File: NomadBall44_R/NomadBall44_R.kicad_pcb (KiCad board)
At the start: 2 copper layers, 147.4 x 96.5 mm, 57 parts, among them SW1 SW_Push, SW10 SW_Push, SW11 SW_Push, SW12 SW_Push, SW13 SW_Push, SW14 SW_Push, SW15 SW_Push, SW16 SW_Push, SW17 SW_Push, SW18 SW_Push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

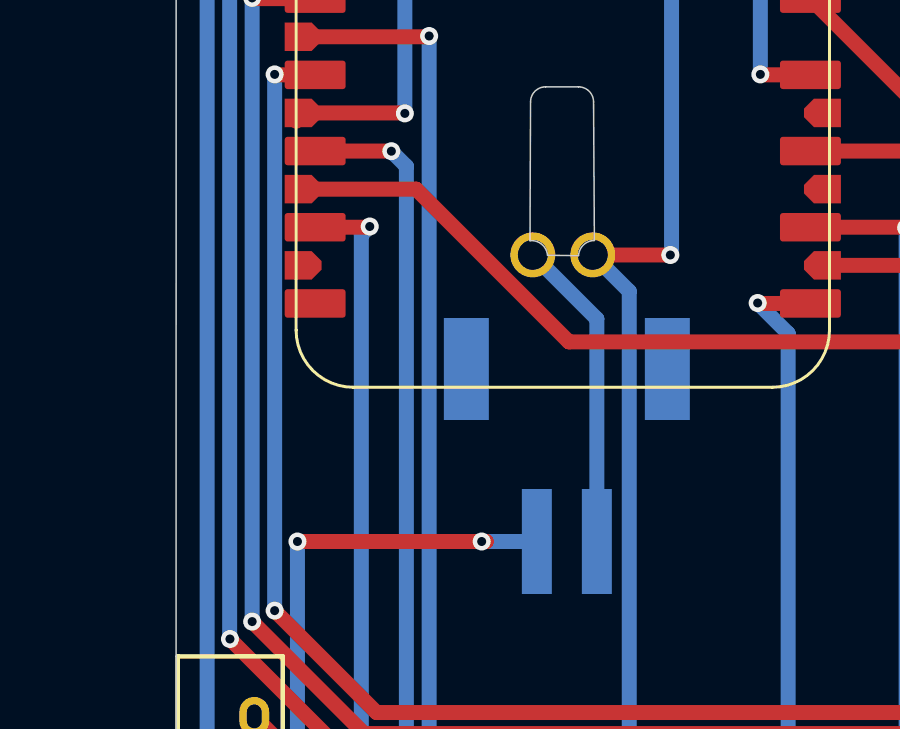
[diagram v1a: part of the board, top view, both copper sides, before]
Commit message: バッテリー周りの配線を修正
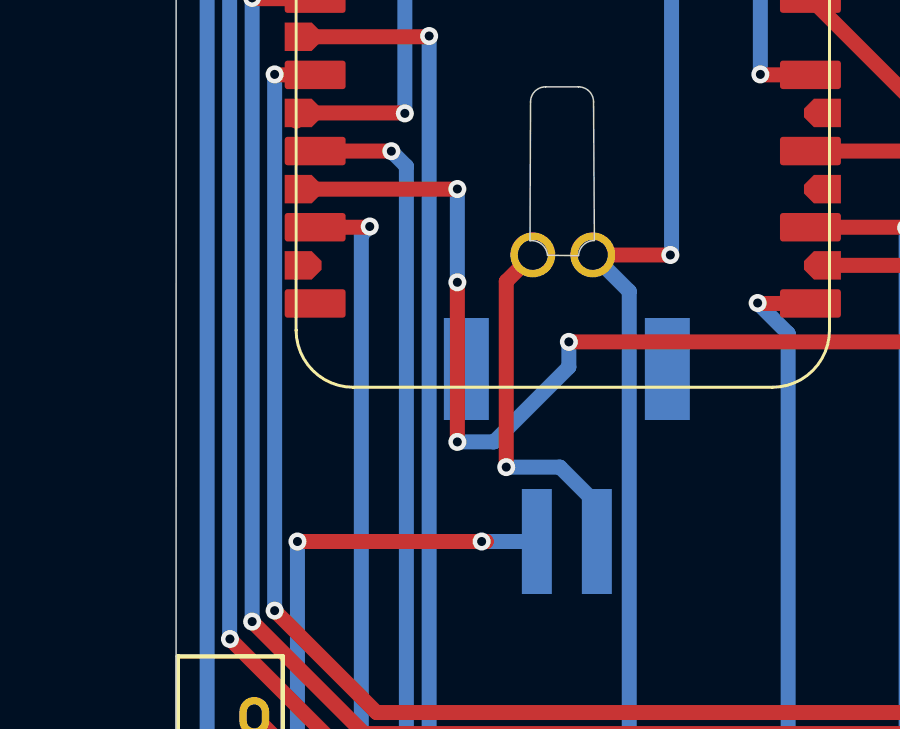
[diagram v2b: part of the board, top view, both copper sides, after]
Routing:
- net Col4: track 150.0 -> 158.2 mm, vias 1 -> 5
- net Bat: track 11.4 -> 13.2 mm, vias 0 -> 1
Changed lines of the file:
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@@
 	)
 	(segment
+		(start 89.98 73.41)
+		(end 89.98 67.22)
+		(width 0.5)
+		(layer "F.Cu")
+		(net 2)
+	)
+	(segment
+		(start 89.98 67.22)
+		(end 90.865 66.335)
+		(width 0.5)
+		(layer "F.Cu")
+		(net 2)
+	)
+	(via
+		(at 89.98 73.41)
+		(size 0.6)
+		(drill 0.3)
+		(layers "F.Cu" "B.Cu")
+		(net 2)
+	)
+	(segment
+		(start 91.77 73.41)
+		(end 89.98 73.41)
+		(width 0.5)
+		(layer "B.Cu")
+		(net 2)
+	)
+	(segment
 		(start 90.865 66.335)
 		(end 90.960327 66.335)
@@
 	)
 	(segment
-		(start 90.985748 66.335)
-		(end 91.103267 66.452519)
+		(start 93 74.64)
+		(end 91.77 73.41)
 		(width 0.5)
 		(layer "B.Cu")
@@
 	)
 	(segment
-		(start 91.103267 66.452519)
-		(end 91.236429 66.588077)
+		(start 90.985748 66.335)
+		(end 91.103267 66.452519)
 		(width 0.5)
 		(layer "B.Cu")
@@
 	)
 	(segment
-		(start 90.865 66.335)
-		(end 90.985748 66.335)
+		(start 93 75.89)
+		(end 93 74.64)
 		(width 0.5)
 		(layer "B.Cu")
@@
 	)
 	(segment
-		(start 93 68.47)
-		(end 93 75.89)
+		(start 91.103267 66.452519)
+		(end 91.236429 66.588077)
 		(width 0.5)
 		(layer "B.Cu")
@@
 	(segment
 		(start 90.865 66.335)
-		(end 93 68.47)
+		(end 90.985748 66.335)
 		(width 0.5)
 		(layer "B.Cu")
@@
 	)
 	(segment
-		(start 86.976529 64.145)
-		(end 92.067529 69.236)
+		(start 88.35 67.25)
+		(end 88.35 72.57)
 		(width 0.5)
 		(layer "F.Cu")
@@
 	)
 	(segment
-		(start 182.427925 67.64)
-		(end 183.58 67.64)
+		(start 83.21 64.145)
+		(end 88.345 64.145)
 		(width 0.5)
 		(layer "F.Cu")
@@
 	)
 	(segment
-		(start 138.196 68.649628)
-		(end 141.145628 65.7)
+		(start 182.427925 67.64)
+		(end 183.58 67.64)
 		(width 0.5)
 		(layer "F.Cu")
@@
 	)
 	(segment
-		(start 83.21 64.145)
-		(end 86.976529 64.145)
+		(start 138.196 68.649628)
+		(end 141.145628 65.7)
 		(width 0.5)
 		(layer "F.Cu")
@@
 		(net 40)
 	)
+	(segment
+		(start 88.345 64.145)
+		(end 88.35 64.14)
+		(width 0.5)
+		(layer "F.Cu")
+		(net 40)
+	)
+	(via
+		(at 92.067529 69.236)
+		(size 0.6)
+		(drill 0.3)
+		(layers "F.Cu" "B.Cu")
+		(net 40)
+	)
+	(via
+		(at 88.35 64.14)
+		(size 0.6)
+		(drill 0.3)
+		(layers "F.Cu" "B.Cu")
+		(net 40)
+	)
+	(via
+		(at 88.35 67.25)
+		(size 0.6)
+		(drill 0.3)
+		(layers "F.Cu" "B.Cu")
+		(net 40)
+	)
+	(via
+		(at 88.35 72.57)
+		(size 0.6)
+		(drill 0.3)
+		(layers "F.Cu" "B.Cu")
+		(net 40)
+	)
 	(via
 		(at 183.58 67.64)
@@
 	)
 	(segment
+		(start 92.067529 70.074471)
+		(end 92.067529 69.236)
+		(width 0.5)
+		(layer "B.Cu")
+		(net 40)
+	)
+	(segment
+		(start 88.35 72.57)
+		(end 89.572 72.57)
+		(width 0.5)
+		(layer "B.Cu")
+		(net 40)
+	)
+	(segment
 		(start 185.031 101.219)
 		(end 183.57 102.68)
@@
 	)
 	(segment
+		(start 89.572 72.57)
+		(end 92.067529 70.074471)
+		(width 0.5)
+		(layer "B.Cu")
+		(net 40)
+	)
+	(segment
 		(start 186.409 80.661)
 		(end 183.57 83.5)
@@
 		(width 0.5)
 		(layer "B.Cu")
+		(net 40)
+	)
+	(segment
+		(start 88.35 64.14)
+		(end 88.35 67.25)
+		(width 0.5)
+		(layer "B.Cu")
